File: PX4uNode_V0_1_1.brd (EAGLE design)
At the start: 45.4 x 34 mm, 129 parts, among them M3_MOUNT1101 MOUNT-HOLE3.1MM, M3_MOUNT1102 MOUNT-HOLE3.1MM, M3_MOUNT1103 MOUNT-HOLE3.1MM, M3_MOUNT1104 MOUNT-HOLE3.1MM, U101 STM32F4X7VX, U401 MAX3051, U402 MAX3051, X101 3.2x2.5 mm / 24 MHz / 15 ppm

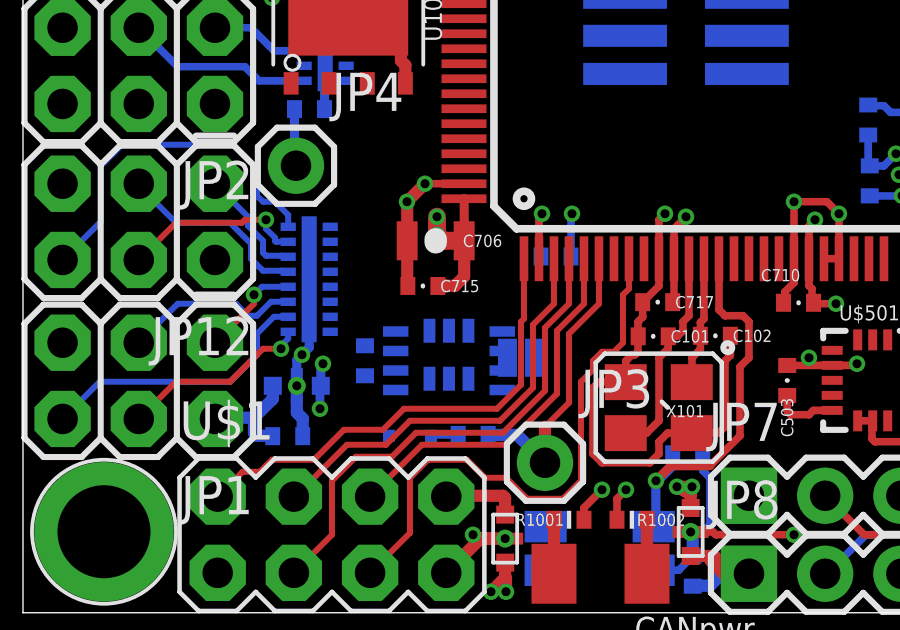
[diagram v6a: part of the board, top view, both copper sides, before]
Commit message: Changed SBUS inverter for TSSOP part with output enable
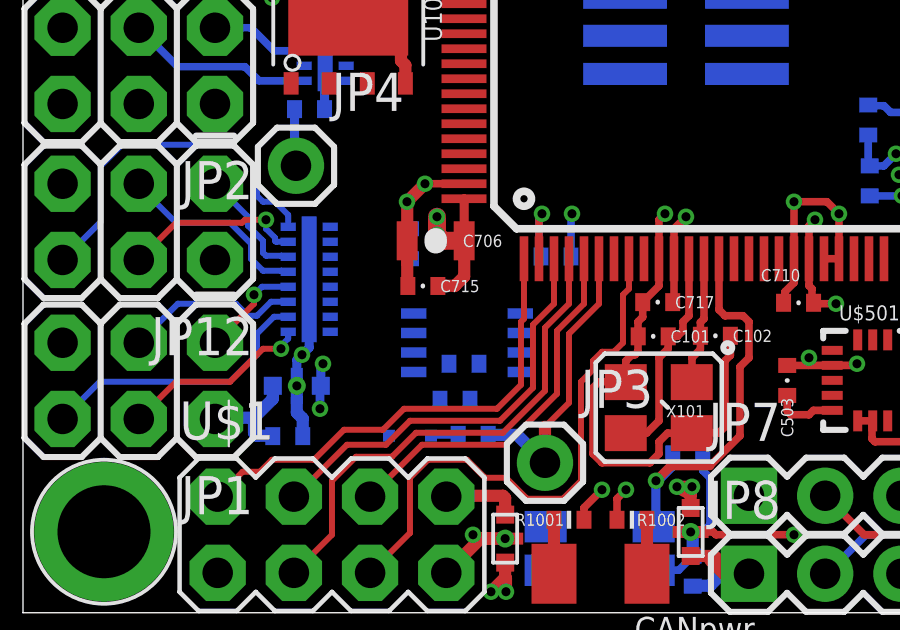
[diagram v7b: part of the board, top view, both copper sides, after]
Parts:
- removed JP202: (no value), SparkFun-Passives:SJ_2S-NO
- removed U$202: 74LVC2GU04, pixhawk2:SOT363_PHILIPS
- added R2, R3: 10K, pixhawk2:0402-RES
- moved C201 4.18 mm to (25.7, 16.5)
- moved U$2 0.85 mm to (27.6, 13.2)
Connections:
- removed net !EX_VDD_5V_VALID: U101.91
- removed net N$5: JP202.1, U$202.4
- new net SBUS_OUTPUT_ENABLE: R3.P$2, U$2.7, U101.91
- net FMU-CH8: now also U$2.3; no longer JP202.2
- net FMU-UART8_RX: now also U$2.6; no longer U$202.6
- net FMU-UART8_TX: now also U$2.5; no longer U$202.3
- net FMU-VDD_3V3: now also R2.P$2, U$2.8; no longer U$202.5
- net GND: now also R2.P$1, R3.P$1, U$2.1, U$2.4; no longer U$202.2
- net PPM_INPUT: now also U$2.2; no longer U$202.1

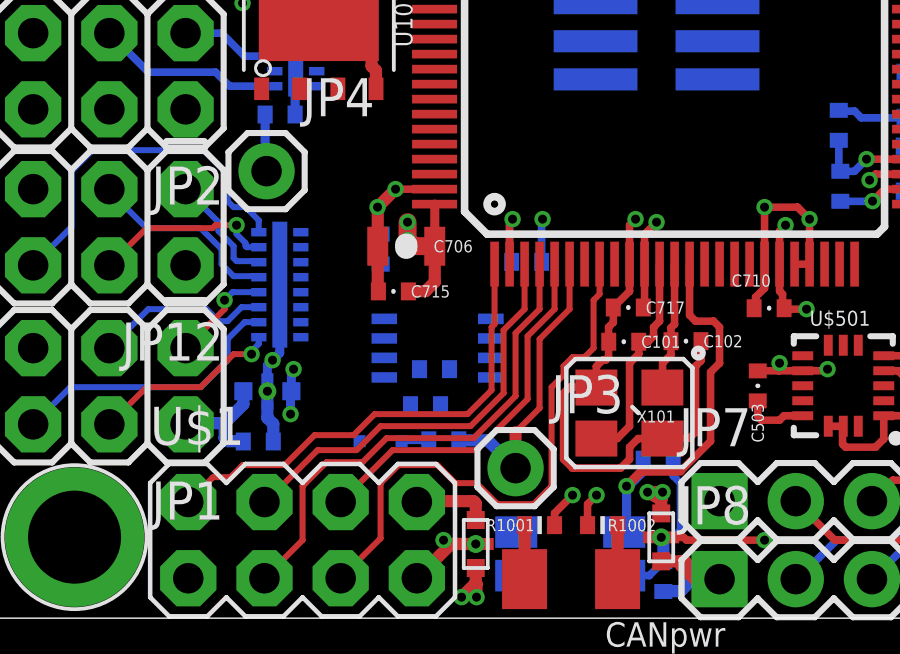
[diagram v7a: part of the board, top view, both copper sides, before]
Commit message: SBUS inverter changed to VSSOP and layout done
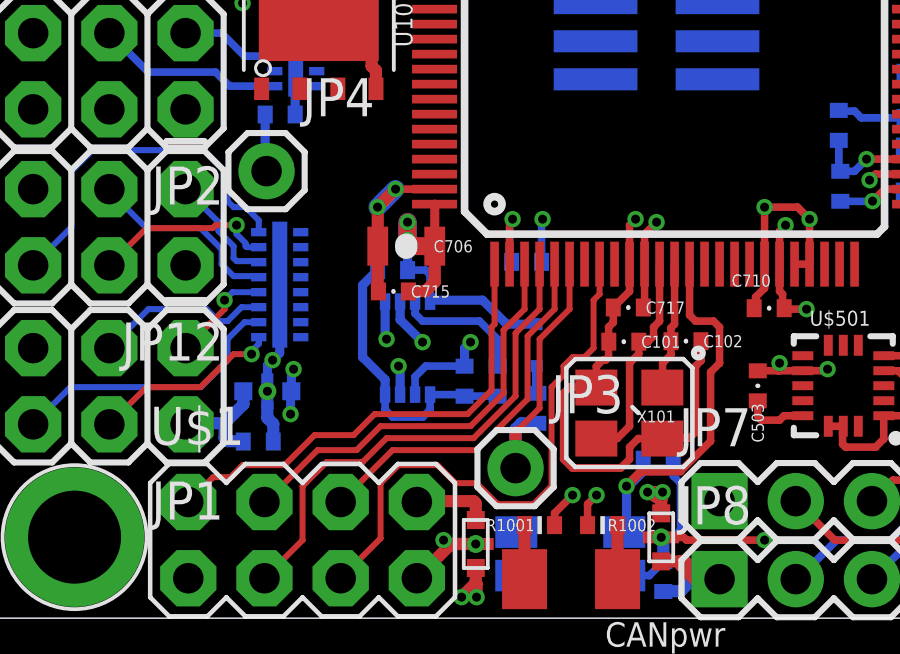
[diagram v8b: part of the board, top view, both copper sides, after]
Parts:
- U$2: value 74LVC2G240-TSSOP-8 -> 74LVC2G240; device pixhawk2:TSSOP8_SOT505-2 -> PX4lite:VSSOP8
- moved D2 6.11 mm to (30.9, 13.3), turned to 270 degrees
- moved R706 3.30 mm to (30.9, 11.2), turned to 90 degrees
- moved R3 2.53 mm to (29.6, 12.1), turned to 90 degrees
- moved R2 1.08 mm to (28.5, 12.1), turned to 270 degrees
- moved U$2 1.00 mm to (26.6, 13.2), turned to 0 degrees
- moved C201 0.81 mm to (26.1, 15.8), turned to 0 degrees
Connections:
- net FMU-VDD_3V3: no longer R2.P$2
- net GND: now also R2.P$2; no longer R2.P$1
- net PPM_INPUT: now also R2.P$1
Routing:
- net GND: track 220.7 -> 233.2 mm
- net FMU-VDD_3V3: track 77.4 -> 84.6 mm
- net SBUS_OUTPUT_ENABLE: track 0.00 -> 4.40 mm
- net PPM_INPUT: track 0.00 -> 3.28 mm, vias 0 -> 1
- net FMU-UART8_RX: track 0.00 -> 1.66 mm, vias 0 -> 1
- net FMU-UART8_TX: track 0.00 -> 1.27 mm, vias 0 -> 1
- net FMU-CH8: track 0.00 -> 0.97 mm, vias 0 -> 1
